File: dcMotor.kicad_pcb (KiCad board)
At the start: 2 copper layers, 145.7 x 97 mm, 67 parts, among them J1 Phoenix Contact 1803426, J2 Conn_01x06_Pin, J3 USB_C_Receptacle_USB2.0_16P, J6 Conn_ST_STDC14, Q2 AO3400A, Q4 MMBT5401, Q5 MMBT5401, SW3 SW_Push, U1 NCP718xSN330, U4 DRV8231ADDA, U5 STM32G0B1CBTx, U7 ER_OLEDM0.91_1x-I2C, U8 LMR54406DBVR, U9 LTH-301-05

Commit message: Wip
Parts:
- added U10: STM32G431RBTx, Package_QFP:LQFP-64_10x10mm_P0.5mm, F.Cu at (82.5, 99.9)

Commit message: moved to G4
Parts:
- removed U5: STM32G0B1CBTx, Package_QFP:LQFP-48_7x7mm_P0.5mm
- moved U10 9.44 mm to (73.2, 100.8), turned to 180 degrees
- moved C7 1.70 mm to (64.0, 103.5)
- moved R3 1.70 mm to (62.5, 103.5)
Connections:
- C11 pad 2: Net-(U5-VREF+) -> Net-(U10-VREF+)
- FB1 pad 2: Net-(U5-VREF+) -> Net-(U10-VREF+)
- U10 pad 1: unconnected-(U10-VBAT-Pad1) -> +3.3V
- U10 pad 10: unconnected-(U10-PC2-Pad10) -> /BUTTON2
- U10 pad 11: unconnected-(U10-PC3-Pad11) -> /BUTTON3
- U10 pad 14: unconnected-(U10-PA2-Pad14) -> /LPUART1_TX
- U10 pad 15: Net-(U10-VSS-Pad15) -> GND
- U10 pad 16: unconnected-(U10-VDD-Pad16) -> +3.3V
- U10 pad 17: unconnected-(U10-PA3-Pad17) -> /LPUART1_RX
- U10 pad 22: unconnected-(U10-PC4-Pad22) -> /BUTTON4
- U10 pad 27: unconnected-(U10-VSSA-Pad27) -> GND
- U10 pad 28: unconnected-(U10-VREF+-Pad28) -> Net-(U10-VREF+)
- U10 pad 29: unconnected-(U10-VDDA-Pad29) -> +3.3V
- U10 pad 31: Net-(U10-VSS-Pad15) -> GND
- U10 pad 32: unconnected-(U10-VDD-Pad32) -> +3.3V
- U10 pad 43: unconnected-(U10-PA9-Pad43) -> /USB_CC1
- U10 pad 44: unconnected-(U10-PA10-Pad44) -> /USB_CC2
- U10 pad 45: unconnected-(U10-PA11-Pad45) -> /USB_D-
- U10 pad 46: unconnected-(U10-PA12-Pad46) -> /USB_D+
- U10 pad 47: Net-(U10-VSS-Pad15) -> GND
- U10 pad 48: unconnected-(U10-VDD-Pad48) -> +3.3V
- U10 pad 49: unconnected-(U10-PA13-Pad49) -> /SWDIO
- U10 pad 50: unconnected-(U10-PA14-Pad50) -> /SWCLK
- U10 pad 51: unconnected-(U10-PA15-Pad51) -> /I2C1_SCL
- U10 pad 57: unconnected-(U10-PB4-Pad57) -> /USB_CC2
- U10 pad 59: unconnected-(U10-PB6-Pad59) -> /USB_CC1
- U10 pad 60: unconnected-(U10-PB7-Pad60) -> /I2C1_SDA
- U10 pad 63: Net-(U10-VSS-Pad15) -> GND
- U10 pad 64: unconnected-(U10-VDD-Pad64) -> +3.3V
- U10 pad 7: unconnected-(U10-PG10-Pad7) -> /NRST
- U10 pad 8: unconnected-(U10-PC0-Pad8) -> /VOUT_EN
- U10 pad 9: unconnected-(U10-PC1-Pad9) -> /BUTTON1
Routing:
- net /USB_CC1: track 21.4 -> 8.08 mm, vias 4 -> 0
- net /USB_D+: track 17.9 -> 6.83 mm, vias 2 -> 0
- net unconnected-(U5-PB10-Pad22): track 8.80 -> 0.00 mm
- net unconnected-(U5-PB11-Pad23): track 8.66 -> 0.00 mm
- net /VBUS_SENSE: track 8.47 -> 0.00 mm
- net /LPUART1_TX: track 8.28 -> 0.00 mm, vias 1 -> 0
- net /USB_D-: track 18.1 -> 11.1 mm, vias 2 -> 0
- net /USB_CC2: track 16.0 -> 9.21 mm, vias 2 -> 0
- net /LPUART1_RX: track 6.47 -> 0.00 mm, vias 1 -> 0
- net +3.3V: track 19.2 -> 13.2 mm
- net /BUTTON3: track 5.79 -> 0.00 mm, vias 2 -> 0
- net Net-(U5-VREF+): track 4.49 -> 0.00 mm
- net GND: track 33.1 -> 30.4 mm, vias 22 -> 21
- net Net-(U10-VREF+): track 0.00 -> 2.50 mm
- net /NRST: track 1.85 -> 0.00 mm, vias 1 -> 0

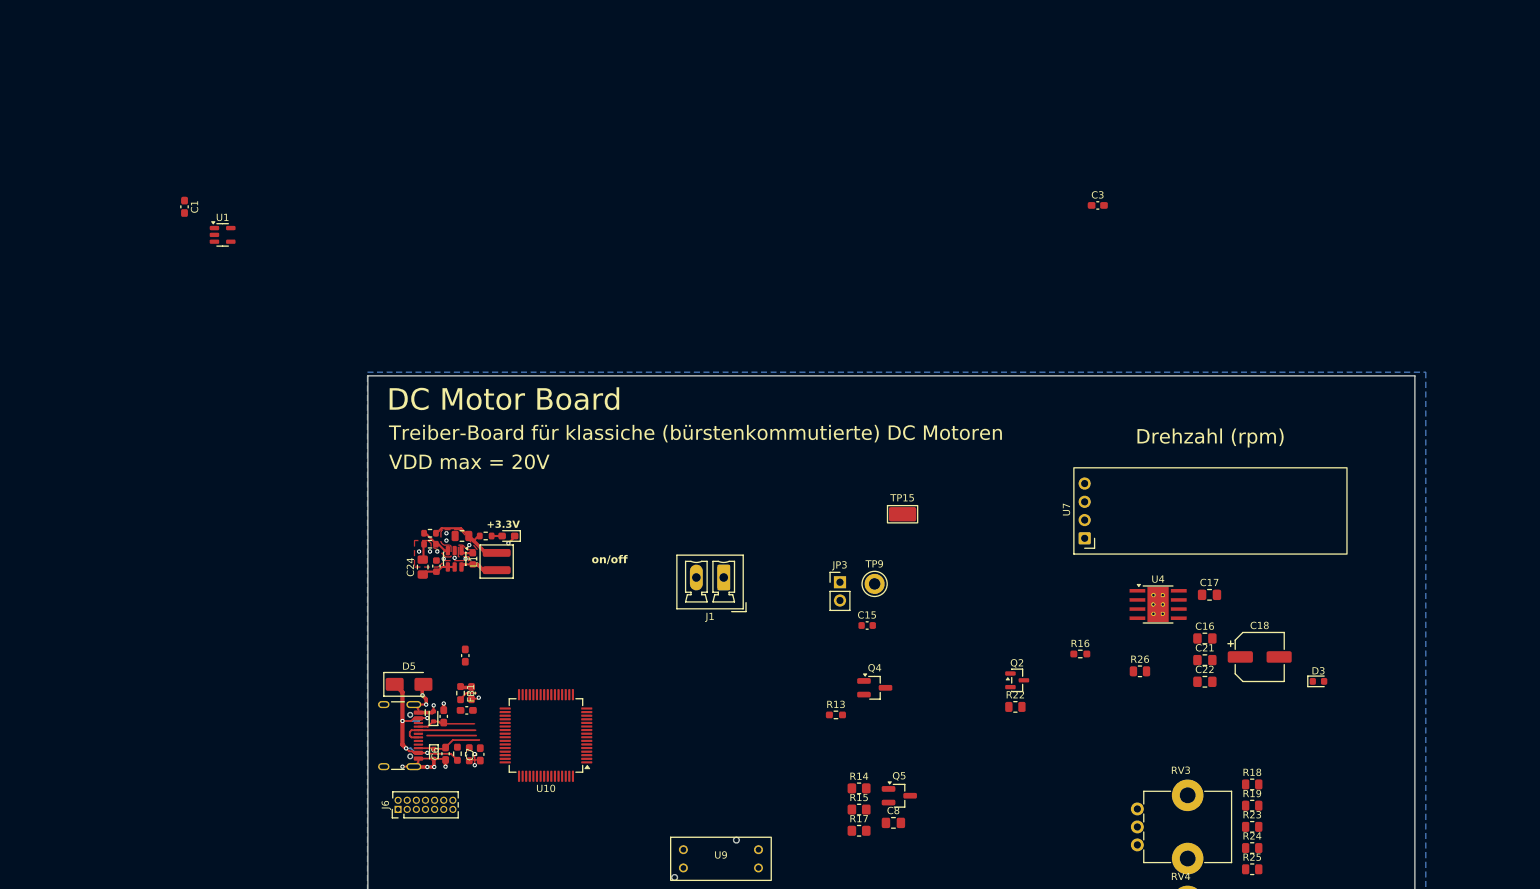
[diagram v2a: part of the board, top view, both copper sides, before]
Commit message: redo PowerSupply designBlock
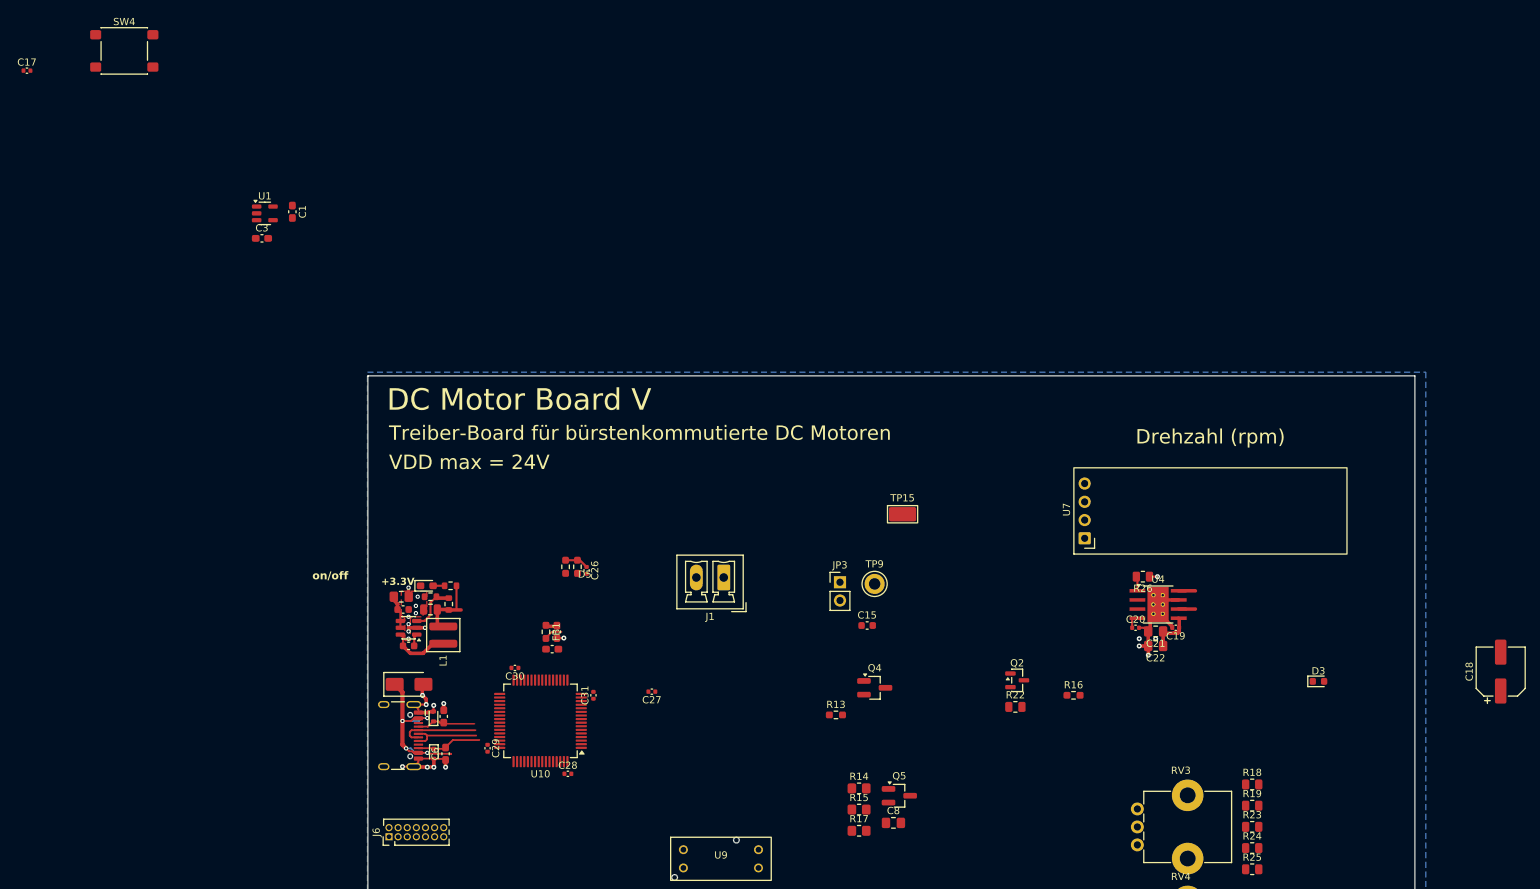
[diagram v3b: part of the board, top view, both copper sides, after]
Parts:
- removed C10: 100n, Capacitor_SMD:C_0603_1608Metric_Pad1.08x0.95mm_HandSolder
- removed C16: 100n, Capacitor_SMD:C_0805_2012Metric_Pad1.18x1.45mm_HandSolder
- removed C7: 1u, Capacitor_SMD:C_0603_1608Metric_Pad1.08x0.95mm_HandSolder
- added C19: 100n, Capacitor_SMD:C_0402_1005Metric, F.Cu at (160.8, 85.9)
- added C20: 100n, Capacitor_SMD:C_0402_1005Metric, F.Cu at (155.2, 85.9)
- added C26: 100n, Capacitor_SMD:C_0402_1005Metric, F.Cu at (78.8, 77.9)
- added C27: 100n, Capacitor_SMD:C_0402_1005Metric, F.Cu at (87.9, 94.7)
- added C28: 100n, Capacitor_SMD:C_0402_1005Metric, F.Cu at (76.2, 106.2)
- added C29: 100n, Capacitor_SMD:C_0402_1005Metric, F.Cu at (65.0, 102.6)
- added C30: 100n, Capacitor_SMD:C_0402_1005Metric, F.Cu at (68.8, 91.4)
- added C31: 100n, Capacitor_SMD:C_0402_1005Metric, F.Cu at (79.8, 95.2)
- added SW4: SW_Push, Button_Switch_SMD:SW_SPST_PTS645Sx43SMTR92, F.Cu at (14.5, 5.59)
- C17: footprint Capacitor_SMD:C_0805_2012Metric_Pad1.18x1.45mm_HandSolder -> Capacitor_SMD:C_0402_1005Metric
- moved C17 180.0 mm to (0.94, 8.34)
- moved C3 116.4 mm to (33.6, 31.7)
- moved C18 33.6 mm to (206.0, 91.9), turned to 90 degrees
- moved R3 30.1 mm to (77.5, 77.4)
- moved R2 30.1 mm to (75.9, 77.4)
- moved C9 15.1 mm to (54.0, 88.4), turned to 0 degrees
- moved C1 15.0 mm to (37.9, 28.0)
- moved C11 14.6 mm to (74.0, 88.8)
- moved C12 14.6 mm to (74.7, 86.4)
- moved FB1 14.6 mm to (73.2, 86.4)
- moved D1 13.3 mm to (56.6, 80.0), turned to 0 degrees
- moved R26 13.2 mm to (156.2, 78.7), turned to 180 degrees
- moved L1 12.6 mm to (58.9, 86.9)
- moved U8 11.5 mm to (54.0, 85.9), turned to 180 degrees
- moved C13 11.1 mm to (57.1, 83.3)
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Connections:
- C14 pad 2: /GPIO_START -> /~{RST}
- C17 pad 2: +3.3V -> /BUTTON1
- SW3 pad 2: /GPIO_START -> /~{RST}
- U10 pad 7: /NRST -> /~{RST}
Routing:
- net GND: track 30.4 -> 45.7 mm, vias 21 -> 23
- net VBUS: track 33.0 -> 37.9 mm
- net /VBUS_SENSE: track 0.00 -> 3.50 mm
- net /USB_D+: track 6.83 -> 9.96 mm
- net Net-(U8-SW): track 5.38 -> 8.31 mm
- net Net-(U8-FB): track 4.39 -> 6.93 mm
- net /MOTOR-: track 0.00 -> 2.31 mm
- net /MOTOR+: track 0.00 -> 2.31 mm
- net /IPROPI: track 0.00 -> 2.03 mm
- net +3.3V: track 13.2 -> 13.8 mm
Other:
- board text added: "DC Motor Board V${REVISION}"
- board text added: "Treiber-Board für bürstenkommutierte DC Motoren"
- board text added: "VDD max = 24V"
- board text removed: "DC Motor Board ${REVISION}"
- board text removed: "Franz Patz, 07-2026"
- board text removed: "Treiber-Board für klassiche (bürstenkommutierte) DC Motoren"
- board text removed: "VDD max = 20V"

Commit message: Wip
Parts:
- added TP10: TestPoint, PZ:TP_Keystone_5010-5014_Multipurpose, F.Cu at (151.5, 80.4)
- added TP11: TestPoint, PZ:TP_Keystone_5010-5014_Multipurpose, F.Cu at (151.5, 85.4)

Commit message: Wip
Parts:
- removed TP10, TP11: TestPoint, PZ:TP_Keystone_5010-5014_Multipurpose
- added D6: B240, Diode_SMD:D_SMB, F.Cu at (3.72, 2.27)
- added D7: B240, Diode_SMD:D_SMB, F.Cu at (3.72, 7.83)
- added TP1, TP3: TP_Keystone_5095, PZ:TP_Keystone_5010-5014_Multipurpose, F.Cu at (2.02, 2.02)
- added TP2: TP_Keystone_5095, PZ:TP_Keystone_5010-5014_Multipurpose, F.Cu at (2.02, 7.08)
- moved J6 6.43 mm to (56.4, 118.9), turned to 180 degrees

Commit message: WiP
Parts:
- added L2: 10µ, PZ:IND_SPM4020T-100M-LR, F.Cu at (58.9, 87.1)
- moved Q4 88.8 mm to (39.4, 54.6)
- moved L1 0.40 mm to (59.2, 87.1)

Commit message: Wip Photointerruptor
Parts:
- added C32: 100n, Capacitor_SMD:C_0402_1005Metric, F.Cu at (108.9, 126.1)
- added R27: 3.3k, Resistor_SMD:R_0805_2012Metric, F.Cu at (93.9, 125.9)
- added R28: 1k, Resistor_SMD:R_0805_2012Metric, F.Cu at (1.71, 3.92)
- added R29: 1k, Resistor_SMD:R_0805_2012Metric, F.Cu at (1.71, 6.88)
- added U5: MCP6561-OT, Package_TO_SOT_SMD:SOT-23-5, F.Cu at (105.7, 125.0)
- R22: value 10k -> 220R
- moved RV4 90.2 mm to (65.3, 133.8)
- moved R22 51.6 mm to (93.9, 122.9)
- moved Q2 50.5 mm to (98.6, 123.7)
- moved C14 45.9 mm to (140.2, 144.8)
- moved SW3 38.9 mm to (137.4, 137.4)
- moved J2 30.4 mm to (121.4, 163.8)
- moved U9 1.74 mm to (99.2, 117.9)
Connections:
- Q2 pad 1: unconnected-(Q2-G-Pad1) -> /EN_PHOTO
- R22 pad 2: unconnected-(R22-Pad2) -> +3.3V
- U10 pad 25: unconnected-(U10-PB1-Pad25) -> /EN_PHOTO
- U9 pad A: +3.3V -> Net-(R22-Pad1)
- U9 pad C: Net-(R22-Pad1) -> /PHOTO_OUT
- U9 pad E: unconnected-(U9-PadE) -> GND

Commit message: added 3Dmodel to local prj
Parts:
- added J4: Conn_Staubli_SLB4-F6,3-rot, PZ:Staubli_SLB4-F6,3-rot, F.Cu at (228.2, 46.9)
- added J5: Conn_Staubli_SLB4-F6,3, PZ:Staubli_SLB4-F6,3-schwarz, F.Cu at (228.2, 60.1)
- added REF**: na, PZ:na, F.Cu at (110.1, 119.4)
- added RV5: PTV09A-1020F-B203, PZ:Potentiometer_Bourns_PTV09A-1_Single_Vertical, F.Cu at (216.7, 120.6)
- moved C17 242.5 mm to (216.5, 119.6)
- moved D6 242.5 mm to (219.2, 113.5)
- moved D7 242.5 mm to (219.2, 119.1)
- moved R28 242.5 mm to (217.2, 115.2)
- moved R29 242.5 mm to (217.2, 118.1)
- moved SW4 242.5 mm to (230.0, 116.8)
- moved TP1 242.5 mm to (217.6, 113.3)
- moved TP2 242.5 mm to (217.6, 118.3)
- moved TP3 242.5 mm to (217.6, 113.3)
- moved C14 107.7 mm to (237.1, 97.7)
- moved C23 107.7 mm to (252.1, 96.6)
- moved D9 107.7 mm to (252.9, 90.1)
- moved R20 107.7 mm to (252.1, 92.6)
- moved R21 107.7 mm to (252.1, 94.6)
- moved SW3 107.7 mm to (234.3, 90.3)
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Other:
- board text removed: "Drehzahl (rpm)"
